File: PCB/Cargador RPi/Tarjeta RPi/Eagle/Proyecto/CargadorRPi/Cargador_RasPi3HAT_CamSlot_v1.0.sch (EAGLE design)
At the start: 22 parts, among them J2 PIN20X2, U1 MCP3208, X2 22-23-2081

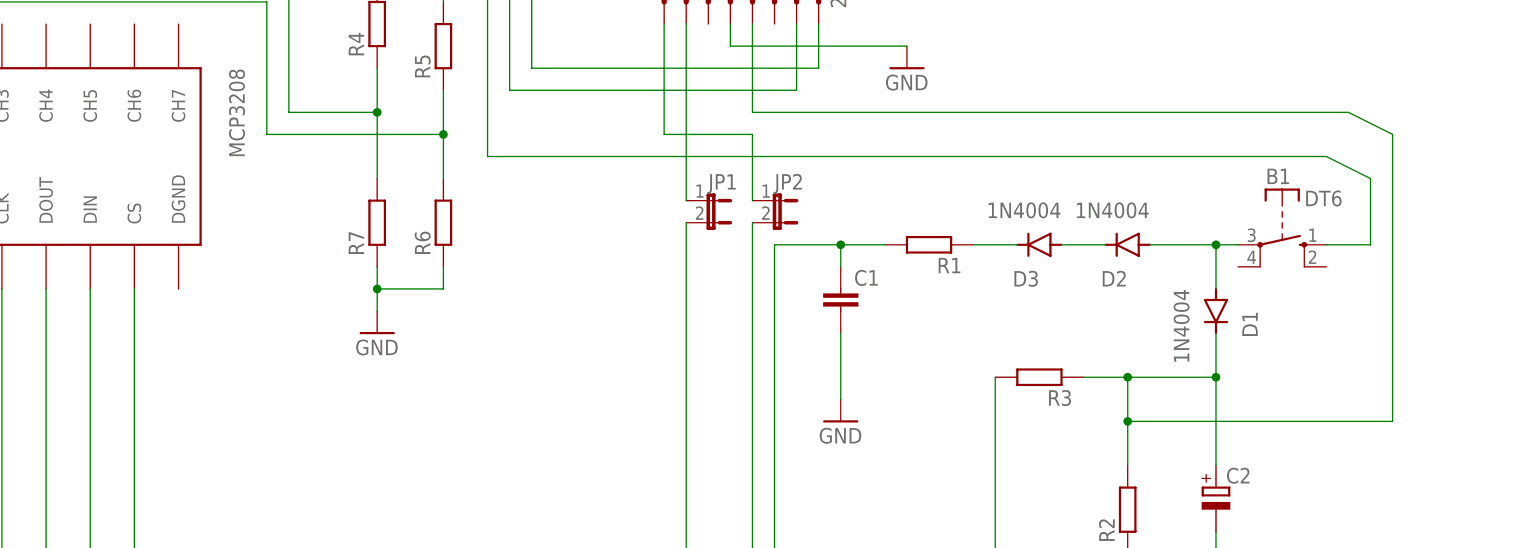
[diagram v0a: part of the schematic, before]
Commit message: Ajustes para fabricación de PCB.
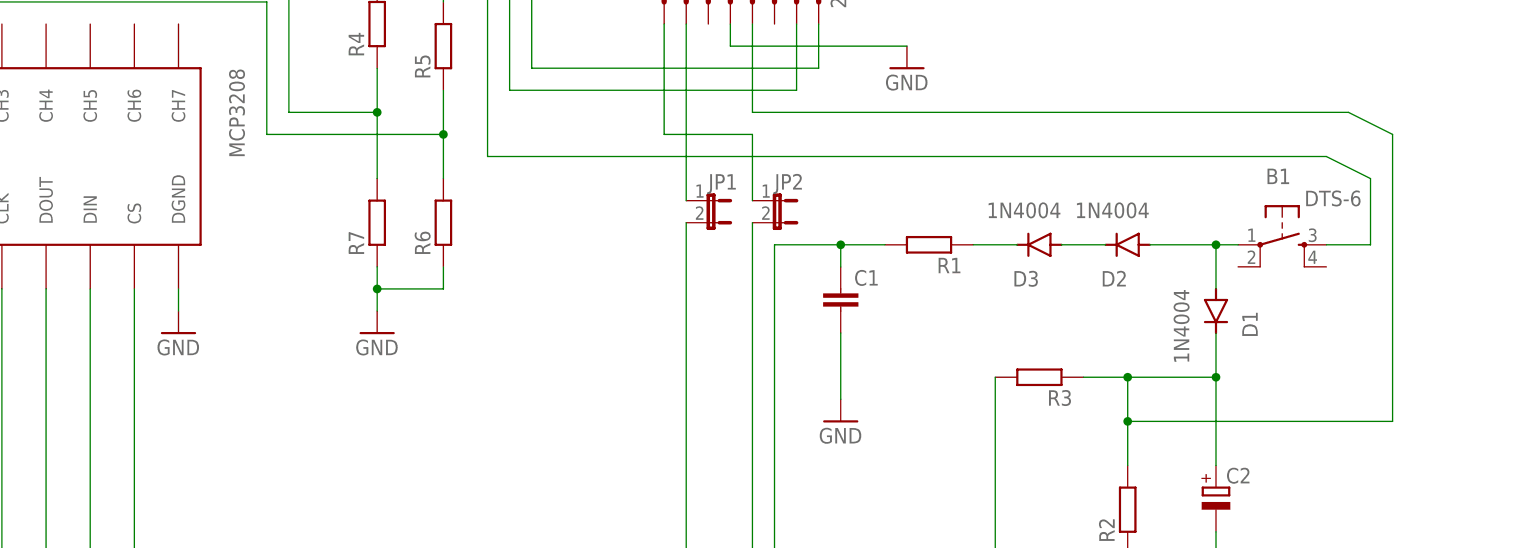
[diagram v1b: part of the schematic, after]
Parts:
- B1: value DT6 -> DTS-6; device switch-misc:DT6 -> switch-tact:DTS-6
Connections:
- net GND: now also U1.DGND
- net N$16: now also B1.3; no longer B1.S
- net N$24: now also B1.1; no longer B1.P
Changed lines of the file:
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@@
 </class>
 <class number="1" name="GND" width="0.254" drill="0">
-<clearance class="1" value="0.127"/>
+<clearance class="1" value="0.381"/>
 </class>
 </classes>
@@
 <part name="C2" library="rcl" library_urn="urn:adsk.eagle:library:334" deviceset="CPOL-EU" device="E5-4" package3d_urn="urn:adsk.eagle:package:23370/1"/>
 <part name="GND13" library="supply1" library_urn="urn:adsk.eagle:library:371" deviceset="GND" device=""/>
-<part name="B1" library="switch-misc" library_urn="urn:adsk.eagle:library:376" deviceset="DT" device="6" package3d_urn="urn:adsk.eagle:package:27430/1"/>
+<part name="B1" library="switch-tact" deviceset="DTS-6" device=""/>
 <part name="GND1" library="supply1" library_urn="urn:adsk.eagle:library:371" deviceset="GND" device=""/>
 <part name="R7" library="rcl" library_urn="urn:adsk.eagle:library:334" deviceset="R-EU_" device="0207/10" package3d_urn="urn:adsk.eagle:package:23491/1"/>
@@
 <part name="R3" library="rcl" library_urn="urn:adsk.eagle:library:334" deviceset="R-EU_" device="0207/10" package3d_urn="urn:adsk.eagle:package:23491/1"/>
 <part name="R1" library="rcl" library_urn="urn:adsk.eagle:library:334" deviceset="R-EU_" device="0207/10" package3d_urn="urn:adsk.eagle:package:23491/1"/>
+<part name="GND2" library="supply1" library_urn="urn:adsk.eagle:library:371" deviceset="GND" device=""/>
 </parts>
 <sheets>
@@
 <attribute name="VALUE" x="251.46" y="160.02" size="1.778" layer="96"/>
 </instance>
-<instance part="B1" gate="1" x="261.62" y="205.74" smashed="yes" rot="R270">
+<instance part="B1" gate="G$1" x="261.62" y="205.74" smashed="yes" rot="R270">
 <attribute name="NAME" x="259.715" y="212.725" size="1.778" layer="95"/>
 <attribute name="VALUE" x="264.16" y="210.185" size="1.778" layer="96"/>
@@
 <attribute name="NAME" x="224.79" y="204.2414" size="1.778" layer="95" rot="R180"/>
 <attribute name="VALUE" x="224.79" y="209.042" size="1.778" layer="96" rot="R180"/>
+</instance>
+<instance part="GND2" gate="1" x="134.62" y="195.58" smashed="yes">
+<attribute name="VALUE" x="132.08" y="193.04" size="1.778" layer="96"/>
 </instance>
 </instances>
@@
 <pinref part="R2" gate="G$1" pin="1"/>
 <wire x1="243.84" y1="165.1" x2="243.84" y2="170.18" width="0.1524" layer="91"/>
+</segment>
+<segment>
+<pinref part="U1" gate="G$1" pin="DGND"/>
+<pinref part="GND2" gate="1" pin="GND"/>
+<wire x1="134.62" y1="200.66" x2="134.62" y2="198.12" width="0.1524" layer="91"/>
 </segment>
 </net>
@@
 <wire x1="266.7" y1="215.9" x2="271.78" y2="213.36" width="0.1524" layer="91"/>
 <wire x1="271.78" y1="213.36" x2="271.78" y2="205.74" width="0.1524" layer="91"/>
-<pinref part="B1" gate="1" pin="S"/>
+<pinref part="B1" gate="G$1" pin="3"/>
 <wire x1="271.78" y1="205.74" x2="266.7" y2="205.74" width="0.1524" layer="91"/>
 <pinref part="R5" gate="G$1" pin="2"/>
@@
 <pinref part="D1" gate="1" pin="A"/>
 <wire x1="254" y1="205.74" x2="254" y2="200.66" width="0.1524" layer="91"/>
-<pinref part="B1" gate="1" pin="P"/>
+<pinref part="B1" gate="G$1" pin="1"/>
 <wire x1="256.54" y1="205.74" x2="254" y2="205.74" width="0.1524" layer="91"/>
 <junction x="254" y="205.74"/>
